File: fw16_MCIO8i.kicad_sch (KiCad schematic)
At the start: 26 parts

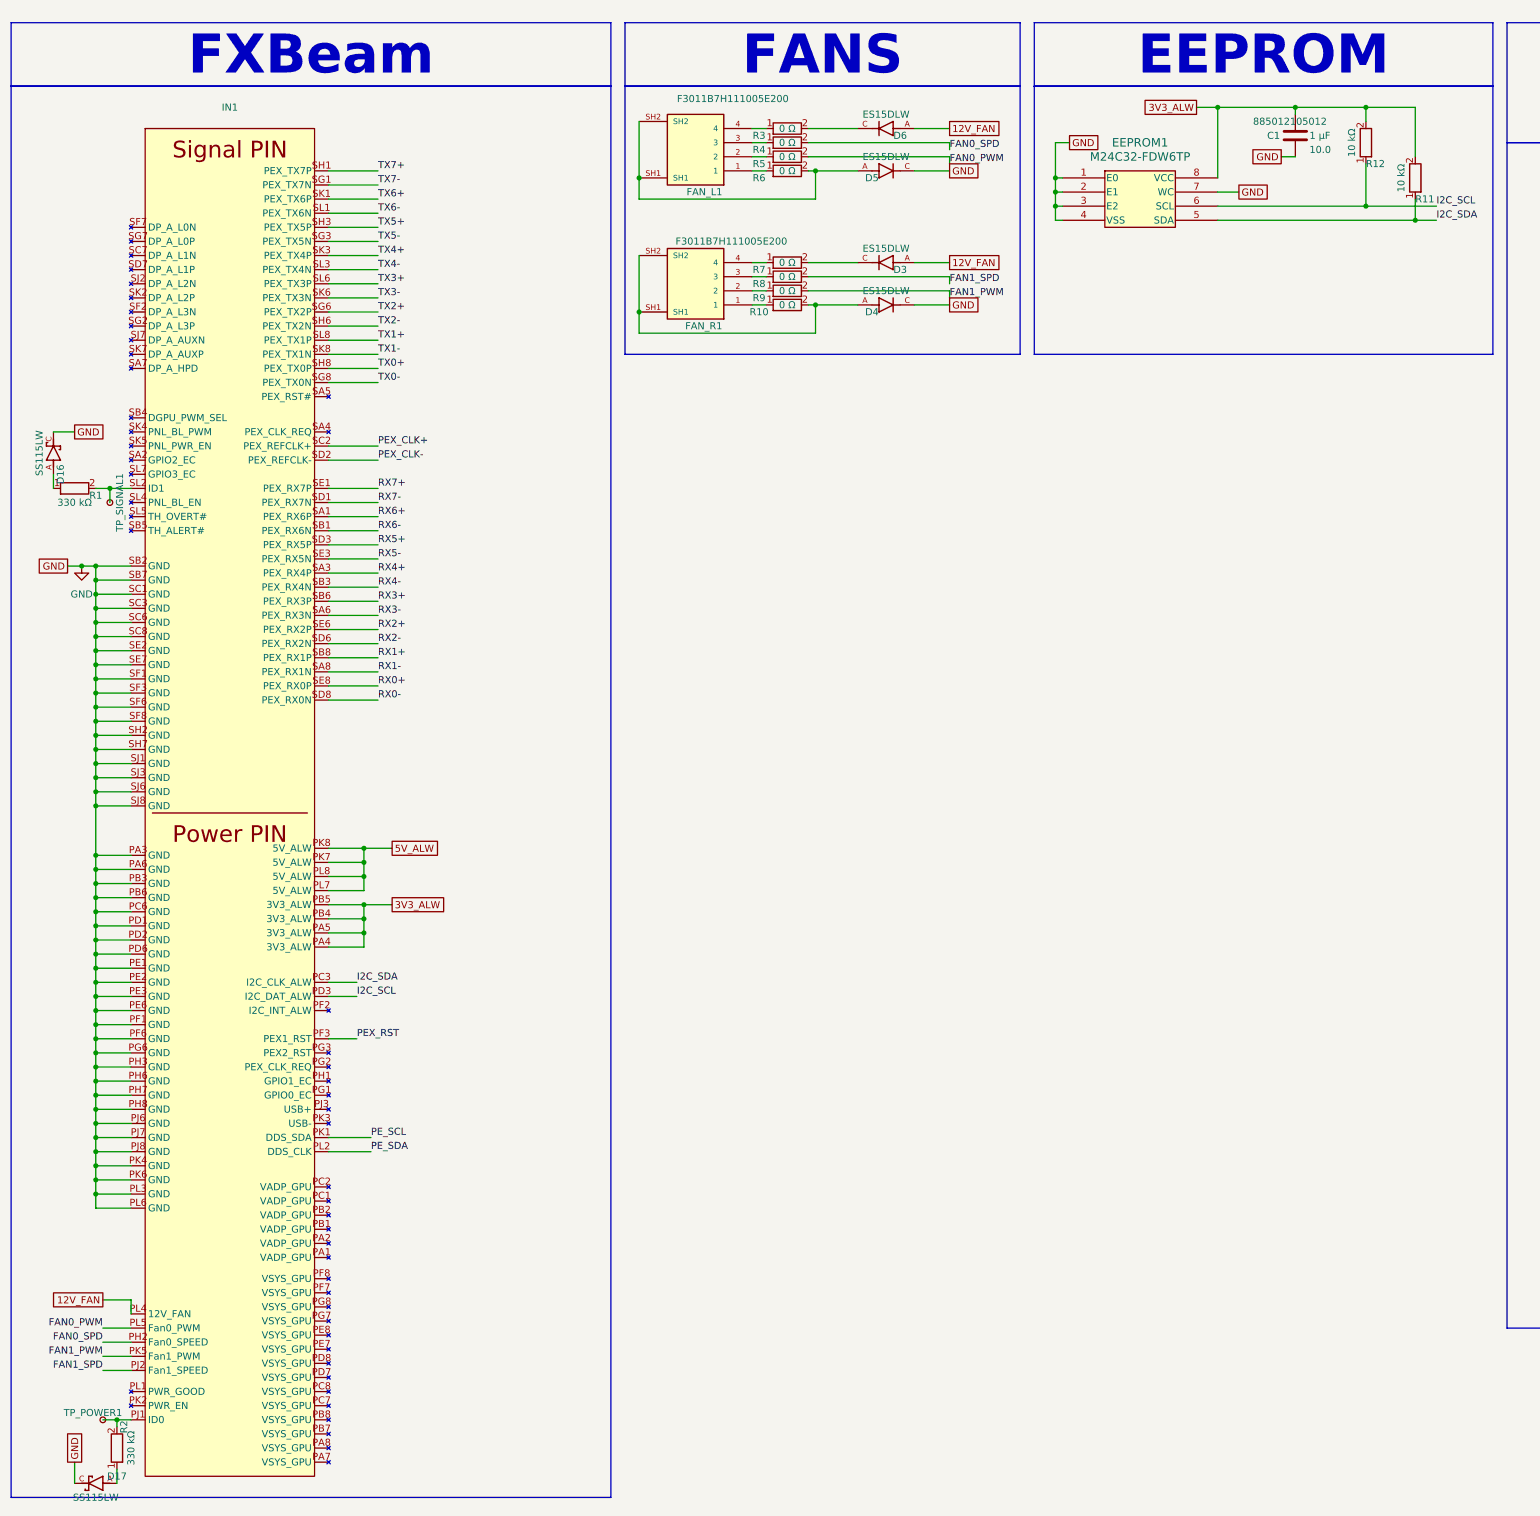
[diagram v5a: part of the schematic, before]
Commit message: MPN added and removed unedded diode
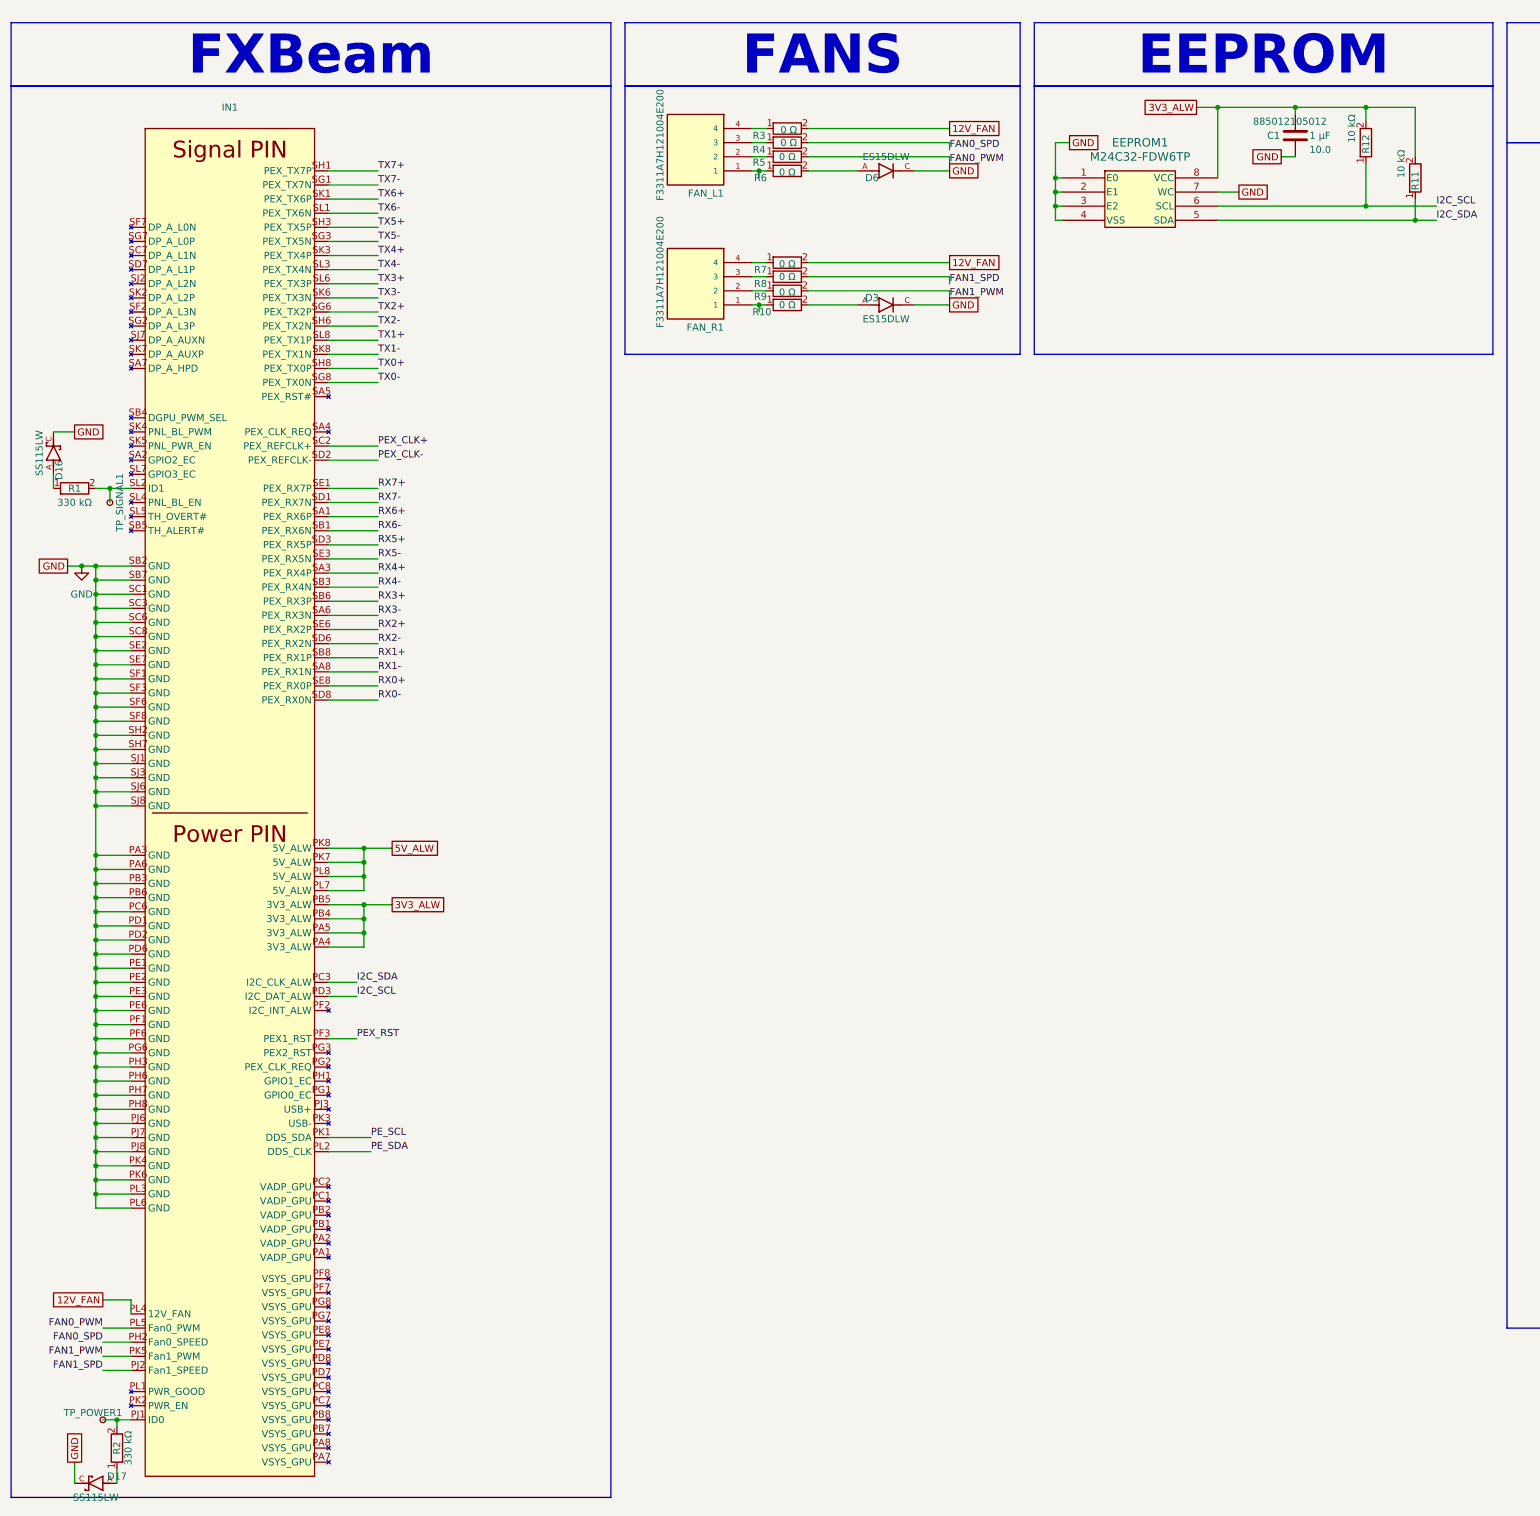
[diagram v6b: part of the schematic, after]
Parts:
- removed D4, D5: ES15DLW, fan-diode:SODFL3718X102N, symbol fan-diode:ES15DLW
- removed FAN_R1: F3011B7H111005E200, fan-connector:AMPHENOL_F33D-1A7H1-E7C04, symbol fan-connector:F33D-1A7H1-E7C04
- added FAN_R1: F3311A7H121004E200, fan-connector:AMPHENOL_F3311A7H121004E200, symbol fan-connector:F3311A7H121004E200
- C1: LCSC Part # (none) -> C6476410; MPN (none) -> 885012105012
- D16, D17: MPN (none) -> SS115LW
- D3, D6: MPN (none) -> ES15DLW
- FAN_L1: value F3011B7H111005E200 -> F3311A7H121004E200; footprint fan-connector:AMPHENOL_F33D-1A7H1-E7C04 -> fan-connector:AMPHENOL_F3311A7H121004E200; symbol fan-connector:F33D-1A7H1-E7C04 -> fan-connector:F3311A7H121004E200; CREATOR ANA -> (none); LCSC Part # (none) -> C3169422; MAXIMUM_PACKAGE_HEIGHT 2.4mm -> 1.62mm; MPN 609-F33D-1A7H1-E7C04CT-ND -> F3311A7H121004E200; PARTREV B -> A; SNAPEDA_PN (none) -> F3311A7H121004E200
- R1: MPN (none) -> 560112132036
- R10, R3, R4, R5, R6, R7, R8, R9: LCSC Part # (none) -> C25268462; MPN (none) -> 560112132007
- R11, R12: LCSC Part # (none) -> C28703254; MPN (none) -> 560112132018
- R2: LCSC Part # (none) -> C28703254; MPN (none) -> 560112132036
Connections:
- net 12V_FAN: now also R3.2, R7.2; no longer D3.A, D6.A
- net GND: now also D3.C, D6.C
- net at R8.1: now also FAN_R1.3
- net at R10.1: now also FAN_R1.1
- net at R9.1: now also FAN_R1.2
- net at R7.1: now also FAN_R1.4
- net at R10.2: now also D3.A
- new net: D6.A, R6.2
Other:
- moved on the sheet: D3, D6

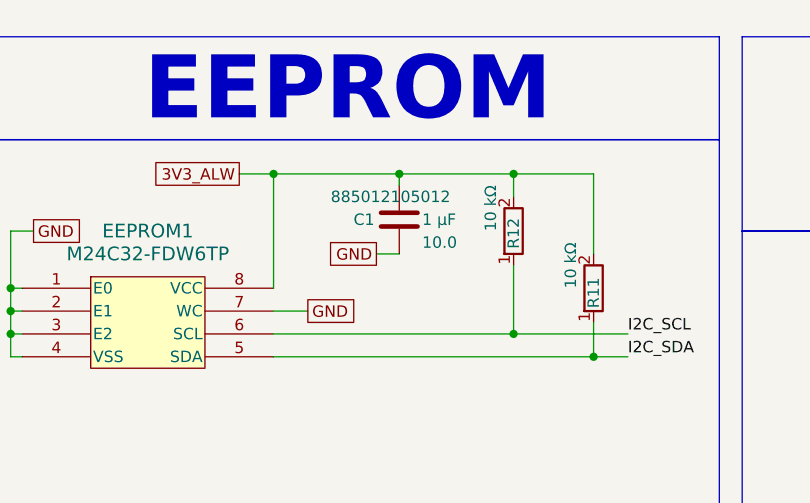
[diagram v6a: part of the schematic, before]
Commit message: Switched capacitor
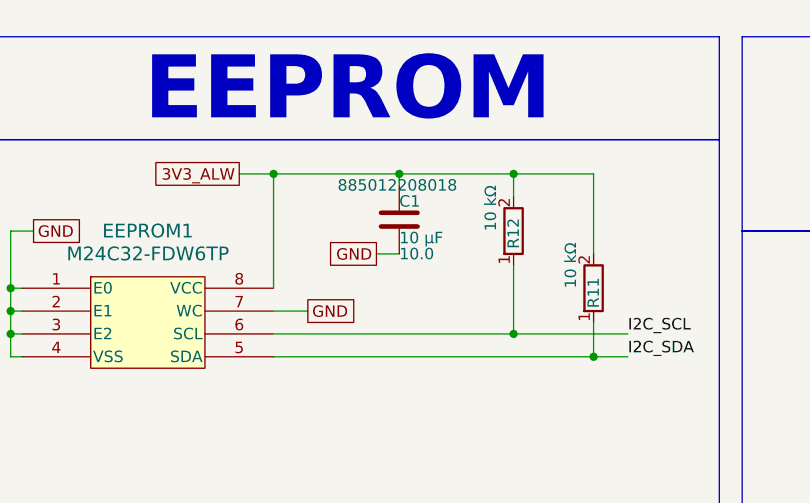
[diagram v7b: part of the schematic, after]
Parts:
- removed C1: 0402_885012105012, capacitor:C_Wurth_WCAP-CSGP-0402, symbol capacitor:0402_885012105012
- added C1: 1206_H1.6_885012208018, capacitor:C_Wurth_WCAP-CSGP-1206_H0.8, symbol capacitor:1206_H1.6_885012208018
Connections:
- net 3V3_ALW: now also C1.1
- net GND: now also C1.2

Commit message: MPN & LCSC
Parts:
- C1: footprint capacitor:C_Wurth_WCAP-CSGP-1206_H0.8 -> capacitor:C_Wurth_WCAP-CSGP-1206_H1.6; LCSC Part # (none) -> C2178587; MPN (none) -> 885012208018
- EEPROM1: LCSC Part # (none) -> C2061249
- MCIO1: LCSC Part # (none) -> C4499806
- R1: LCSC Part # (none) -> C26798316
- R2: LCSC Part # C28703254 -> C26798316
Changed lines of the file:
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@@
 			)
 		)
-		(property "LCSC Part #" "C28703254"
+		(property "LCSC Part #" "C26798316"
 			(at 35.56 273.05 0)
 			(effects
@@
 		)
 		(property "MPN" "560112132036"
+			(at 27.94 100.33 0)
+			(effects
+				(font
+					(size 1.27 1.27)
+				)
+				(hide yes)
+			)
+		)
+		(property "LCSC Part #" "C26798316"
 			(at 27.94 100.33 0)
 			(effects
@@
 			)
 		)
+		(property "LCSC Part #" "C2061249"
+			(at 219.71 42.164 0)
+			(effects
+				(font
+					(size 1.27 1.27)
+				)
+				(hide yes)
+			)
+		)
 		(pin "7"
 		)
@@
 			)
 		)
-		(property "Footprint" "capacitor:C_Wurth_WCAP-CSGP-1206_H0.8"
+		(property "Footprint" "capacitor:C_Wurth_WCAP-CSGP-1206_H1.6"
 			(at 252.73 16.51 0)
 			(effects
@@
 				)
 				(justify left)
+			)
+		)
+		(property "MPN" "885012208018"
+			(at 247.65 36.83 0)
+			(effects
+				(font
+					(size 1.27 1.27)
+				)
+				(hide yes)
+			)
+		)
+		(property "LCSC Part #" "C2178587"
+			(at 247.65 36.83 0)
+			(effects
+				(font
+					(size 1.27 1.27)
+				)
+				(hide yes)
 			)
 		)
@@
 			(effects
 				(font
+					(size 1.27 1.27)
+				)
+				(hide yes)
+			)
+		)
+		(property "LCSC Part #" "C4499806"
+			(at 344.17 106.68 0)
+			(effects
+				(font
